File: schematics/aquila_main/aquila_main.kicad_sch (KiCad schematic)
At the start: 131 parts, among them IC1 MS5611-01BA03, J1 120591-1, J10 PYRO_3, J11 PYRO_2, J12 PYRO_4, J13 AudioJack3_SwitchTR, J14 SERVO, J2 1043P, J3 1043P, J4 PWR, J5 TELEM, J6 GPS, J7 BARO, J8 BMI-S-201, J9 PYRO_1, Q1 IRF7509PbF, Q2 IRF7509PbF, Q3 IRF7509PbF, Q4 IRF7509PbF, U1 LM2576S-3.3/NOPB, U2 LM2576D2TR4-5G, U3 MAX-M8Q, U4 Si4463, U5 B3520, U6 SKY65723-11, U7 ADXL357, U8 BQ29200, U9 Teensy4.1, Y1 30M

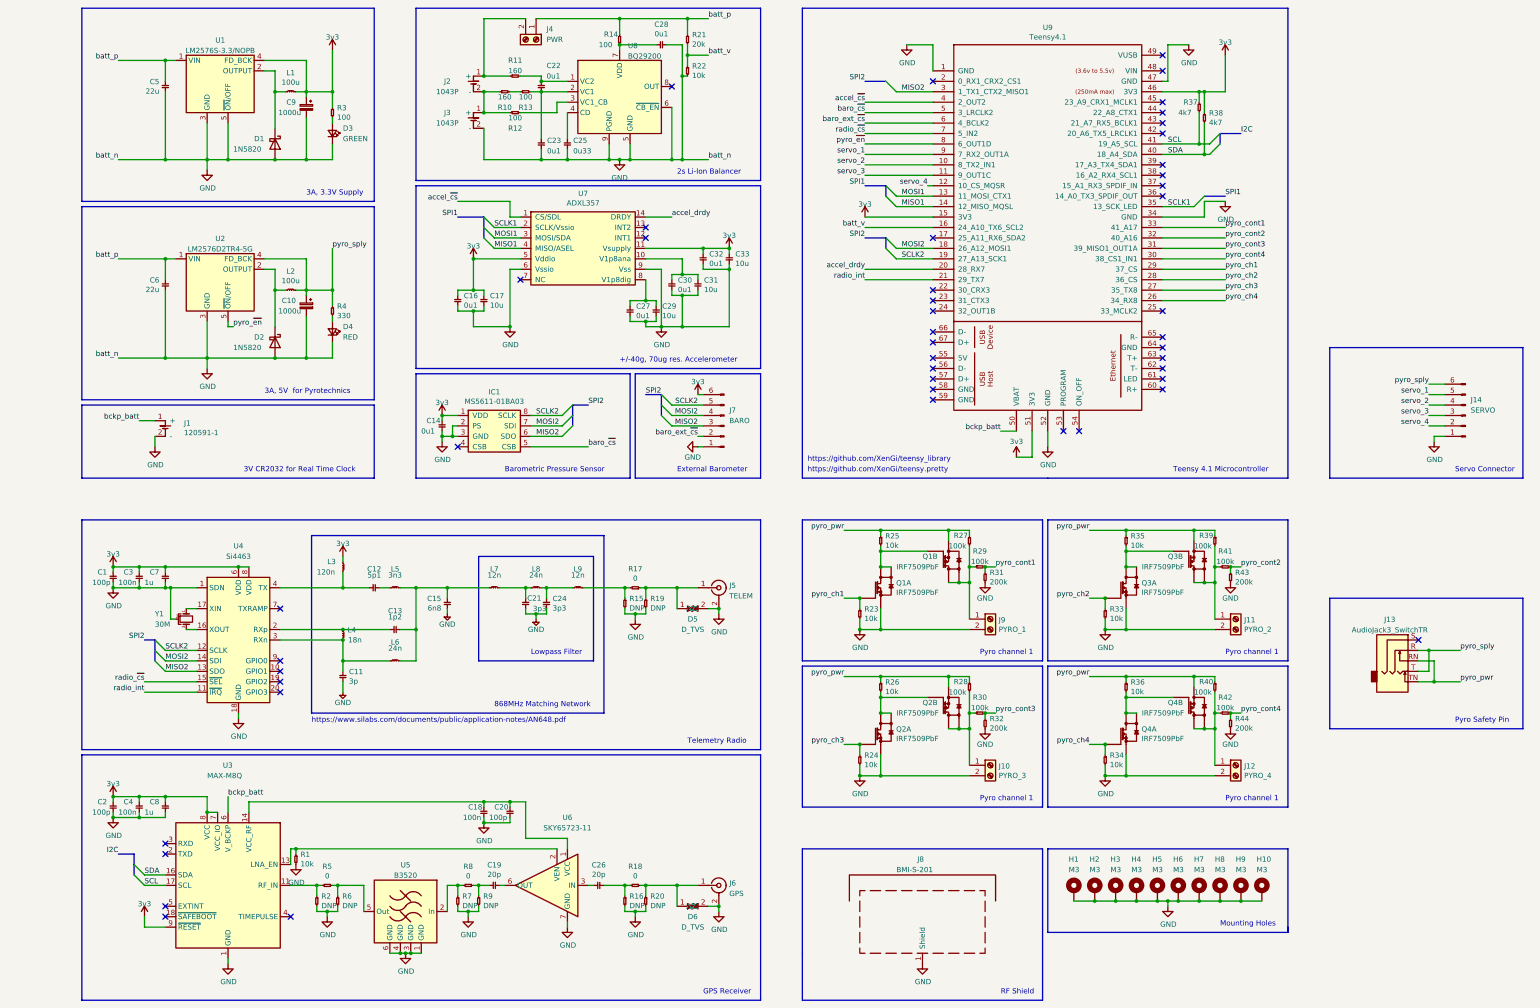
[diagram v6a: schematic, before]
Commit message: added test points, redesigned power supplies
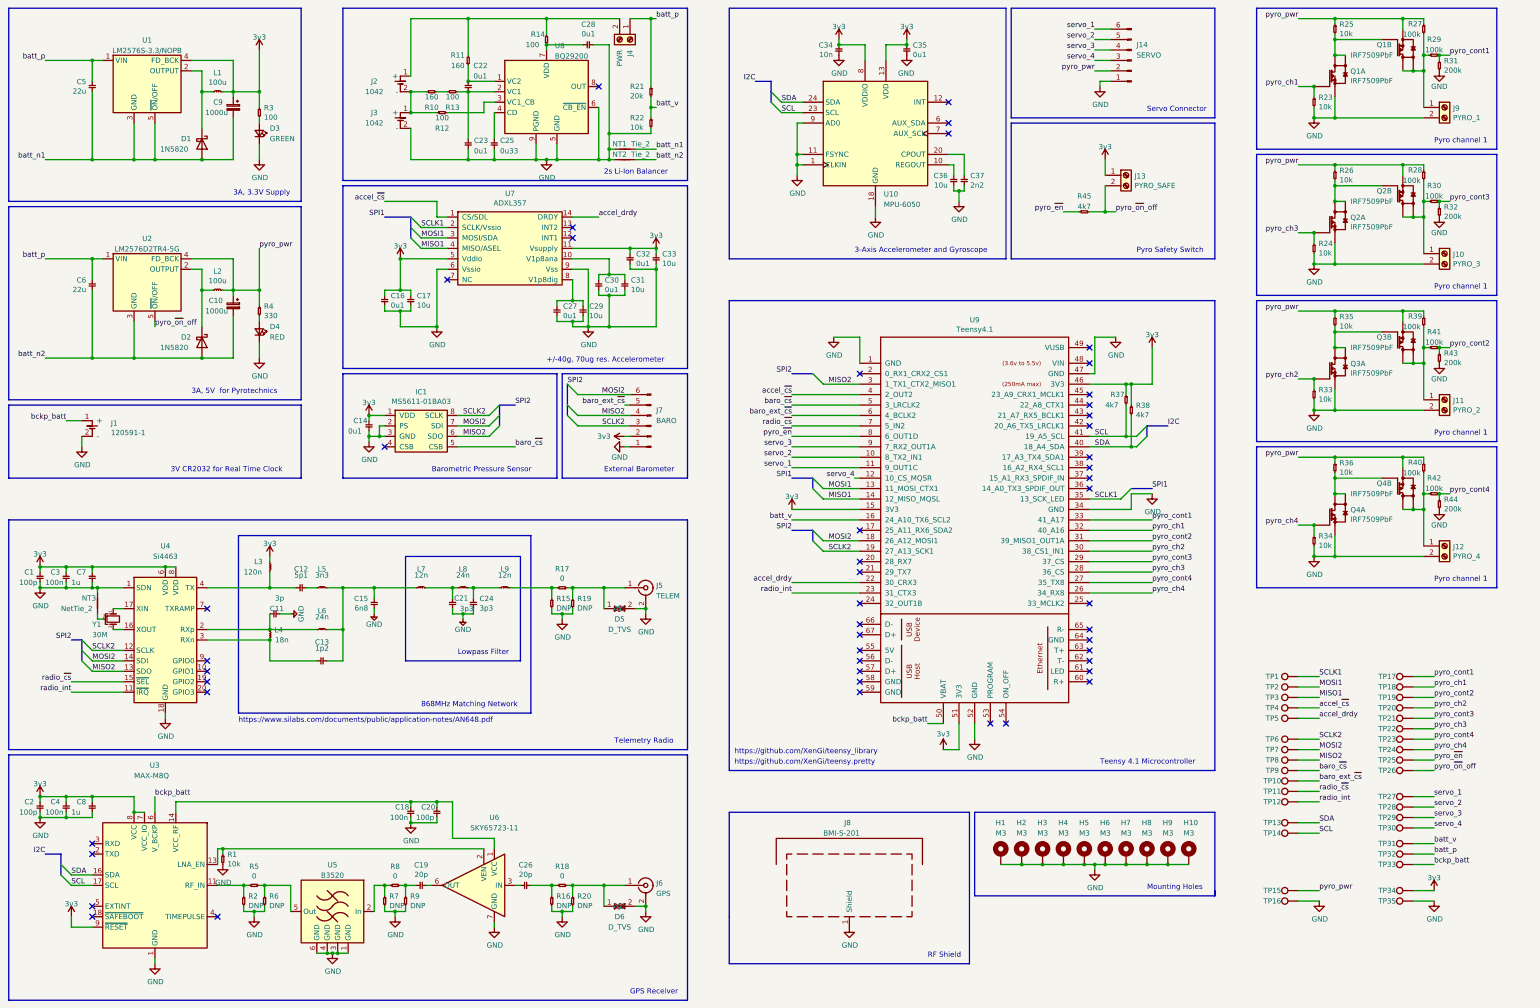
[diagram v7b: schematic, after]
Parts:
- removed J13: AudioJack3_SwitchTR, aquila:audio_2.5mm_1501_02, symbol Connector:AudioJack3_SwitchTR
- added C34: 10n, Capacitor_SMD:C_0402_1005Metric, symbol aquila:C-cusf-kicad
- added C35: 0u1, Capacitor_SMD:C_0402_1005Metric, symbol aquila:C-cusf-kicad
- added C36: 10u, Capacitor_SMD:C_0402_1005Metric, symbol aquila:C-cusf-kicad
- added C37: 2n2, Capacitor_SMD:C_0402_1005Metric, symbol aquila:C-cusf-kicad
- added J13: PYRO_SAFE, aquila:MP_2.54_screw_terminal_2x1, symbol Connector:Screw_Terminal_01x02
- added NT1, NT2: Tie_2, NetTie:NetTie-2_THT_Pad1.0mm, symbol Device:NetTie_2
- added NT3: NetTie_2, NetTie:NetTie-2_SMD_Pad0.5mm, symbol Device:NetTie_2
- added R45: 4k7, Resistor_SMD:R_0402_1005Metric, symbol aquila:R-cusf-kicad
- added TP1, TP10, TP11, TP12, TP13, TP14, TP15, TP16, TP17, TP18, TP19, TP2, TP20, TP21, TP22, TP23, TP24, TP25, TP26, TP27, TP28, TP29, TP3, TP30, TP31, TP32, TP33, TP34, TP35, TP4, TP5, TP6, TP7, TP8, TP9: TestPoint, TestPoint:TestPoint_Pad_D1.0mm, symbol Connector:TestPoint
- added U10: MPU-6050, Sensor_Motion:InvenSense_QFN-24_4x4mm_P0.5mm, symbol Sensor_Motion:MPU-6050
- C5, C6: footprint Capacitor_SMD:C_0402_1005Metric -> Capacitor_THT:CP_Radial_D6.3mm_P2.50mm; Farnell (none) -> 9452710
- D5: footprint aquila:DO-214AA -> Diode_SMD:D_0402_1005Metric; Farnell 1797898 -> 2368169
- D6: footprint aquila:DO-214AA -> Diode_SMD:D_0402_1005Metric; Farnell (none) -> 2368169
- J2, J3: value 1043P -> 1042; footprint aquila:1043 -> aquila:1042
- L1, L2: Farnell 3370508 -> 2288307
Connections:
- net +3V3: now also J7.2 (Pin_2), C34.1, C35.1, J13.1 (Pin_1), TP34.1, U10.13 (VDD), U10.8 (VDDIO); no longer J7.6 (Pin_6)
- net GND: now also C34.2, C35.2, C36.2, C37.2, NT1.1, NT2.1, NT3.2, TP16.1, TP35.1, U10.1 (CLKIN), U10.11 (FSYNC), U10.18 (GND), U10.9 (AD0); no longer C10.2, C5.2, C6.2, C9.2, D1.2 (A), D2.2 (A), U1.3 (GND), U1.5 (~{ON}/OFF), U2.3 (GND), Y1.2
- net MISO1: now also TP3.1
- net MISO2: now also J7.4 (Pin_4), TP8.1; no longer J7.3 (Pin_3)
- net MOSI1: now also TP2.1
- net MOSI2: now also J7.6 (Pin_6), TP7.1; no longer J7.4 (Pin_4)
- net SCL: now also TP14.1, U10.23 (SCL)
- net SCLK1: now also TP1.1
- net SCLK2: now also J7.3 (Pin_3), TP6.1; no longer J7.5 (Pin_5)
- net SDA: now also TP13.1, U10.24 (SDA)
- net accel_drdy: now also U9.22 (30_CRX3), TP5.1; no longer U9.20 (28_RX7)
- net accel_~{cs}: now also TP4.1
- net baro_ext_~{cs}: now also J7.5 (Pin_5), TP10.1; no longer J7.2 (Pin_2)
- net baro_~{cs}: now also TP9.1
- net batt_p: now also TP32.1; no longer R14.2
- net batt_v: now also TP31.1
- net bckp_batt: now also TP33.1
- net pyro_ch1: now also U9.32 (40_A16), TP18.1; no longer U9.29 (37_CS)
- net pyro_ch2: now also U9.30 (38_CS1_IN1), TP20.1; no longer U9.28 (36_CS)
- net pyro_ch3: now also U9.28 (36_CS), TP22.1; no longer U9.27 (35_TX8)
- net pyro_ch4: now also TP24.1
- net pyro_cont1: now also TP17.1
- net pyro_cont2: now also U9.31 (39_MISO1_OUT1A), TP19.1; no longer U9.32 (40_A16)
- net pyro_cont3: now also U9.29 (37_CS), TP21.1; no longer U9.31 (39_MISO1_OUT1A)
- net pyro_cont4: now also U9.27 (35_TX8), TP23.1; no longer U9.30 (38_CS1_IN1)
- net pyro_pwr: now also C10.1, J14.2 (Pin_2), L2.2, R4.1, U2.4 (FD_BCK), TP15.1
- net pyro_~{en}: now also R45.1, TP25.1; no longer U2.5 (~{ON}/OFF)
- net radio_int: now also U9.23 (31_CTX3), TP12.1; no longer U9.21 (29_TX7)
- net radio_~{cs}: now also TP11.1
- net servo_1: now also J14.6 (Pin_6), U9.11 (9_OUT1C), TP27.1; no longer J14.5 (Pin_5), U9.9 (7_RX2_OUT1A)
- net servo_2: now also J14.5 (Pin_5), TP28.1; no longer J14.4 (Pin_4)
- net servo_3: now also J14.4 (Pin_4), U9.9 (7_RX2_OUT1A), TP29.1; no longer J14.3 (Pin_3), U9.11 (9_OUT1C)
- net servo_4: now also J14.3 (Pin_3), TP30.1; no longer J14.2 (Pin_2)
- net at L4.1, U4.2 (RXp): now also C11.1, L6.1; no longer C13.1
- net at L4.2, U4.3 (RXn): now also C13.1; no longer C11.1, L6.1
- net at C22.2, U8.1 (VC2): now also R11.1; no longer R11.2
- net at J2.1 (+), J4.2 (Pin_2): now also R11.2, R14.2; no longer R11.1
- removed net pyro_sply: C10.1, J14.6 (Pin_6), L2.2, R4.1, U2.4 (FD_BCK)
- new net: NT3.1, Y1.2
- new net: C37.1, U10.20 (CPOUT)
- new net: C36.1, U10.10 (REGOUT)
- new net batt_n1: C5.2, C9.2, D1.2 (A), NT1.2, U1.3 (GND), U1.5 (~{ON}/OFF)
- new net batt_n2: C10.2, C6.2, D2.2 (A), NT2.2, U2.3 (GND)
- new net pyro_~{on}_off: J13.2 (Pin_2), R45.2, TP26.1, U2.5 (~{ON}/OFF)
- no-connect marks 47 -> 49
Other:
- note added: "3-Axis Accelerometer and Gyroscope"
- note added: "Pyro Safety Switch"
- note removed: "Pyro Safety Pin"
- moved on the sheet: C1, C10, C11, C12, C13, C14, C15, C16, C17, C18, C19, C2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

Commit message: added manufacture files and BoM
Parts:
- C21, C24: Farnell 3013357 -> 2627406
- J14, J7: DigiKey (none) -> WM16880-ND
- J2, J3: DigiKey 36-1043P-ND -> 36-1042P-ND
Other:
- note added: "Test Points"
- moved on the sheet: TP1, TP10, TP11, TP12, TP13, TP14, TP15, TP16, TP17, TP18, TP19, TP2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
